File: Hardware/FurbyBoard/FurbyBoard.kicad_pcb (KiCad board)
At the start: 4 copper layers, 68.8 x 74.6 mm, 154 parts, among them J1 USB-C 16P, J11 J_EXP: header de expansión 2 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, J2 BAT+, J3 BAT-, J5 Micro I2S (SD, GND, SCK, WS, 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, J6 FPC 24P 0.5, J7 Frente: IR (emisor ×2, recept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, J8 Inclinación ×3, lengua ×2, al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, J9 Encoder ×3, leva ×2, barriga 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, Q1 SI7615ADN, Q3 AO3400A, SW1 RESET, SW2 BOOT, U1 USBLC6-2SC6, U10 TCA9535PWR, U11 SN74LVC1G17DBVR, U2 BQ24073RGTR, U3 TPS63802DLAR, U4 ESP32-S3-WROOM-1-N16R8, U5 TPS61089RNRR, U6 DRV8231ADSGR, U7 MAX98357AETE+T, U8 ME6211C28M5G-N, U9 ME6211C12M5G-N

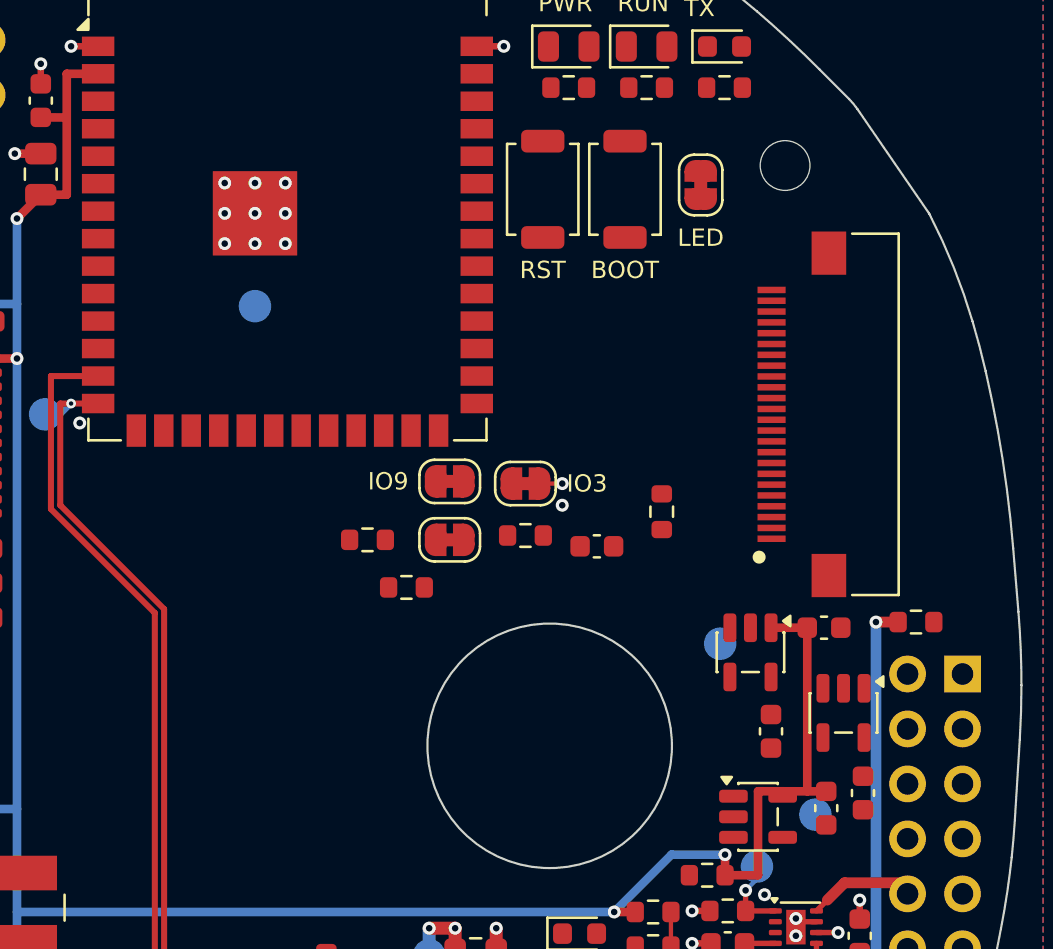
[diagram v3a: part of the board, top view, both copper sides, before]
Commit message: Feature: rutado del bus DVP de la cámara y del abanico de J6
Bus DVP J6 -> U4 en F.Cu, rutado de río sin cruces: Y2-Y5 en escalera
entre SW1 y la columna de pads a los pines 31-34; los ocho restantes
bajan a 45° a una banda de paso 0,3 (y -81,8…-83,9) y entran en los
pines 18-25 por orden. Los pines no DVP de J6 salen por el este bajo el
cuerpo a una columna de vías (GND, DVDD, PWDN, SCL, SDA, GND) o por el
oeste (2V8, RST a R35/C31); 3V3 del pin 11, de R35 y de R18 por una
fila de In2 hasta la vía de R35 y por B.Cu a U8.1. CAM_DVDD por In2
bordeando J9 hasta U9.5/C29 (TP11 en B); CAM_2V8 por In2 a U8.5/C28 y
U9.1 (TP10 en B); CAM_EN con sus vías junto a U8.3 y U9.3; BOOT de pin
27 a R18 y por In2 a SW2. Retorno de GND a <= 1 mm en cada vía CAM_*.

Colocación: JP1/JP2 en fila bajo la banda (y -85,1), JP3 a 270° al
este, R29/R30 debajo, R18 junto al pin 27, C31 junto a R35, SW1/SW2
0,4/0,2 mm al este para dejar paso a la escalera; C29 alineado con
U9.5. Puentes de soldadura: IPROPI_IO/MOT_IN*_IO desde los pines 15-17
por In2 y B.Cu (IPROPI_IO), IPROPI por In2 (x -54,7) a JP3.

DRU: cuello de 0,15 dentro del patio de J6 (pads de 0,3 a 0,5 mm de
paso, como J1), para que el 3V3 del pin 11 y el bus de 0,15 pasen.

Puerta D: DRC 0 con paridad 0 (5 avisos de vías pendientes de unir en
los bloques siguientes), revisar-rutado 0 errores, PNG revisados del
pasillo de la cámara (F, In2, B) y de la zona J6/U8/U9.

Co-Authored-By: Claude Fable 5.1 <noreply@anthropic.com>
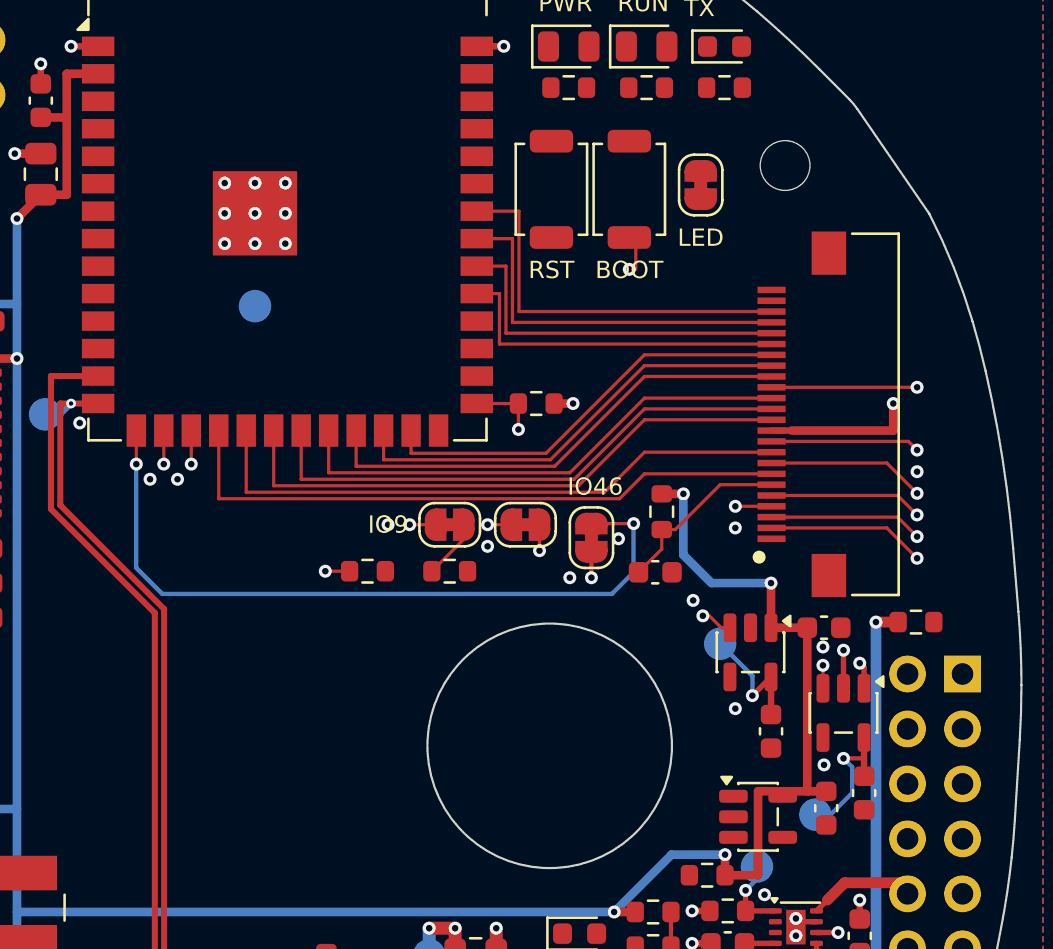
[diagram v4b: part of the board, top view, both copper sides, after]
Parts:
- moved R18 6.12 mm to (158.5, 39.5)
- moved R29 4.07 mm to (154.5, 47.2)
- moved JP3 3.94 mm to (161.1, 45.7), turned to -90 degrees
- moved JP2 3.57 mm to (158.0, 45.1)
- moved C31 2.95 mm to (164.0, 47.3)
- moved JP1 2.00 mm to (154.5, 45.1)
- moved R30 1.95 mm to (150.7, 47.2)
- moved SW1 0.40 mm to (159.2, 29.6)
- moved SW2 0.20 mm to (162.8, 29.6)
- moved C29 0.05 mm to (173.7, 57.5)
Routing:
- net 3V3: track 172.7 -> 209.9 mm, vias 10 -> 14
- net IPROPI_IO: track 0.00 -> 34.4 mm, vias 0 -> 2
- net CAM_DVDD: track 0.00 -> 29.7 mm, vias 0 -> 2
- net CAM_VSYNC: track 0.00 -> 29.2 mm
- net CAM_HREF: track 0.00 -> 27.9 mm
- net CAM_Y9: track 0.00 -> 26.8 mm
- net CAM_2V8: track 0.00 -> 26.4 mm, vias 0 -> 3
- net CAM_XCLK: track 0.00 -> 25.3 mm
- net CAM_Y8: track 0.00 -> 23.8 mm
- net CAM_Y7: track 0.00 -> 22.6 mm
- net CAM_PCLK: track 0.00 -> 21.1 mm
- net MOT_IN2_IO: track 0.00 -> 21.1 mm, vias 0 -> 2
- net CAM_Y6: track 0.00 -> 19.6 mm
- net CAM_Y4: track 0.00 -> 18.3 mm
- net CAM_Y3: track 0.00 -> 17.5 mm
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
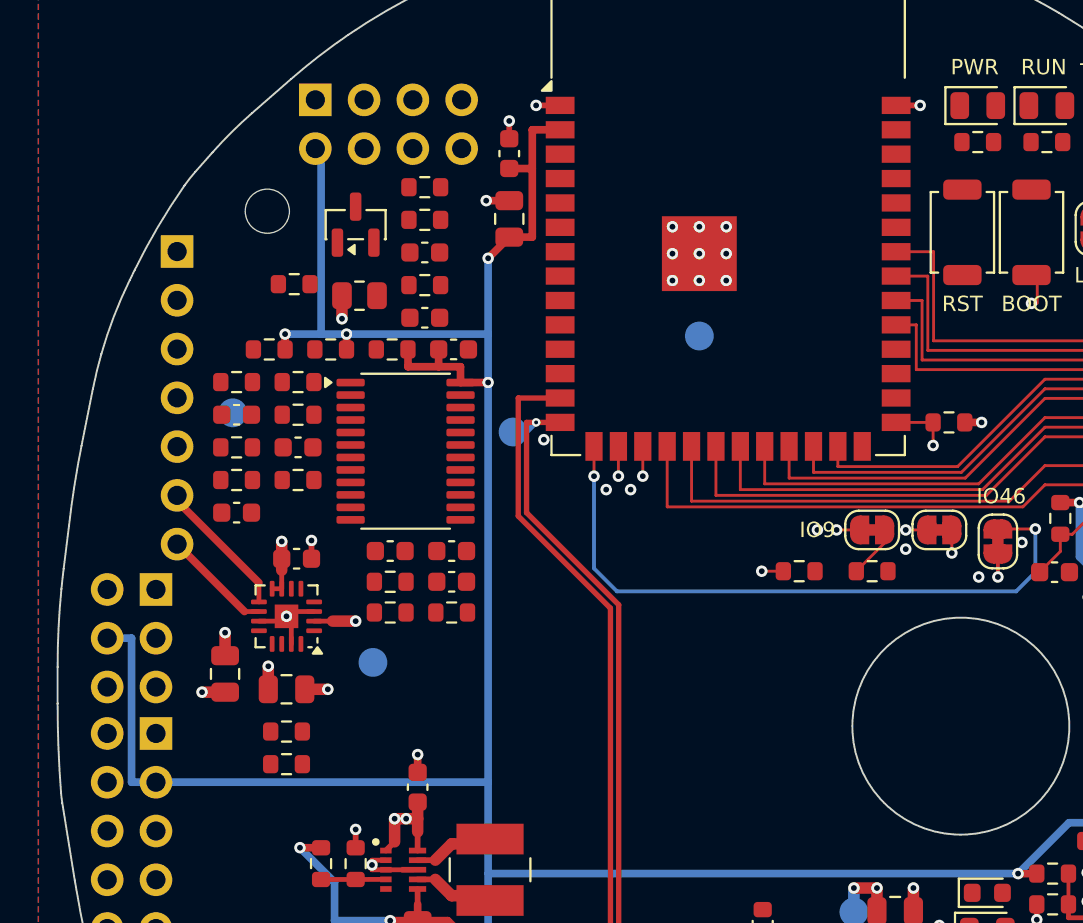
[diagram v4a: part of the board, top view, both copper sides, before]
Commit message: Feature: rutado del I2S, el I2C, EXP_INT, EN y AMP_SD de la FurbyBoard
Los pines 3-10 de la columna oeste del módulo bajan a vías bajo el
cuerpo (o al oeste del pad en WS y DIN) con retorno de GND. I2S por In2
en cuatro columnas anidadas y filas y -87,0…-88,2 hasta J5.1 (DIN),
U7.14 (WS, vía bajo C25 desde el oeste), U7.16 (BCLK, vía al este de
C25) y U7.1 (DOUT, TP9 en B); BCLK y WS siguen en F.Cu a R31/R32 (a
180°) y SCK_MIC/WS_MIC en F.Cu a J5.3/J5.4 (WS_MIC bordea J5 y J11 por
el oeste). I2C por In2 a U10.22/23 (vías al este del tronco de B.Cu)
y por B.Cu a R36/R37 (intercambiados para que las filas aniden);
EXP_INT por In2 (y -66,2, columna x -84,8) a U10.1 y R38.1; EN por In2
a R17/C11 y a SW1; AMP_SD en F.Cu. J7.5 se alimenta de 3V3 por In2
(x -93,85) para dejar libre B.Cu; TP2 bajo el par USB; C25.2 con vía al
sur (retorno de la vía de WS).

Puerta D: DRC 0 con paridad 0 (5 avisos de vías de I2C/CAM pendientes
de unir en el bloque siguiente), revisar-rutado 0 errores, PNG
revisados de la zona oeste (F, In2, B) y de U7/J5 (F, In2).

Co-Authored-By: Claude Fable 5.1 <noreply@anthropic.com>
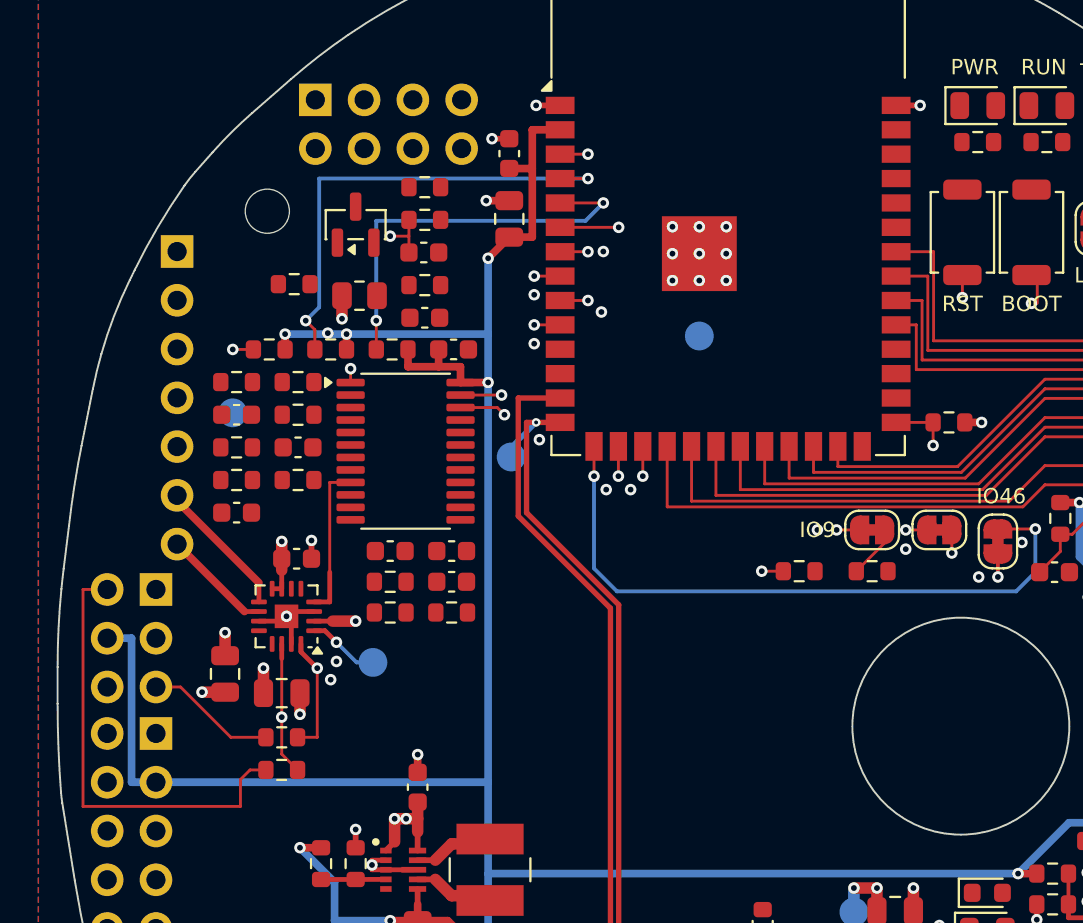
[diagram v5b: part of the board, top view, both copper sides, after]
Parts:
- moved R36 3.20 mm to (126.3, 35.7)
- moved R37 3.20 mm to (129.5, 35.7)
- moved TP2 1.30 mm to (135.7, 41.3)
- moved R31 0.39 mm to (123.8, 55.9), turned to 180 degrees
- moved R32 0.39 mm to (123.8, 57.6), turned to 180 degrees
- moved C25 0.32 mm to (123.8, 53.6)
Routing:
- net EN: track 0.00 -> 51.8 mm, vias 0 -> 3
- net I2S_WS: track 0.00 -> 50.9 mm, vias 0 -> 2
- net I2S_BCLK: track 0.00 -> 43.5 mm, vias 0 -> 2
- net I2C_SDA: track 7.10 -> 48.9 mm, vias 1 -> 4
- net I2C_SCL: track 7.10 -> 45.8 mm, vias 1 -> 4
- net EXP_INT: track 0.00 -> 38.3 mm, vias 0 -> 3
- net I2S_DOUT: track 0.00 -> 36.1 mm, vias 0 -> 2
- net I2S_DIN: track 0.00 -> 35.4 mm, vias 0 -> 1
- net I2S_WS_MIC: track 0.00 -> 23.7 mm
- net AMP_SD: track 0.00 -> 8.12 mm
- net I2S_SCK_MIC: track 0.00 -> 6.81 mm
- net 3V3: track 209.9 -> 210.8 mm, vias 14 -> 15
- net USB_DP: track 57.2 -> 58.1 mm
- net GND: track 68.6 -> 68.4 mm, vias 77 -> 83

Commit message: Feature: rutado del sensado (VBAT_SNS, LIGHT, ENC_PT), VBUS a J11 y BAT_PAD
VBAT_SNS: pin 39 -> vía bajo el módulo, In2 por y -64,26, x -78,0 y
x -80,6 (único paso libre entre las filas del I2S y las vías de los
pines 15-17) y diagonal hasta la vía junto a R13.2; divisor R13/R14/C5
encadenado en F.Cu. LIGHT: pin 38 -> vía, B.Cu por y -64,0 hasta J7.6
(THT) y por In2 a la vía junto a C40.1 (C40 a 180°). ENC_PT: U11.2 <->
R52.1 en F.Cu y vía a In2 por el hueco entre las filas de pads de J9
hasta J9.1. VBUS a J11.4 por B.Cu (diagonal larga bajo los
convertidores). BAT_PAD de J2 a Q1.5 (0,8). Zona BAT hasta y -112,3
(conexión sólida a los pines 2/3 de U2), C4 al este, vía de GND del
pin 4 de U2 a (-63,6; -113,6), retorno de BQ_TS en (-65,65; -114,45) y
BQ_TS por In2 con salida en diagonal: la zona BAT queda en un solo
polígono. Retorno de GND a <= 1 mm en cada vía de red crítica.

Puerta D: DRC 0 con paridad 0 (5 avisos de vías de I2C/CAM pendientes
de unir), revisar-rutado 0 errores, PNG revisados (NE del módulo, J7,
J9/U11, cargador y VBUS a J11).

Co-Authored-By: Claude Fable 5.1 <noreply@anthropic.com>
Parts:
- moved C4 0.85 mm to (156.1, 74.5)
- turned C40 to 180 degrees
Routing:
- net VBAT_SNS: track 0.00 -> 71.9 mm, vias 0 -> 2
- net LIGHT: track 0.00 -> 45.3 mm, vias 0 -> 2
- net VBUS: track 28.3 -> 54.8 mm
- net ENC_PT: track 0.00 -> 21.0 mm, vias 0 -> 1
- net BAT_PAD: track 0.00 -> 2.44 mm
- net BQ_TS: track 20.8 -> 19.7 mm
- net BAT: track 19.6 -> 18.6 mm
- net GND: track 68.4 -> 68.8 mm, vias 83 -> 87

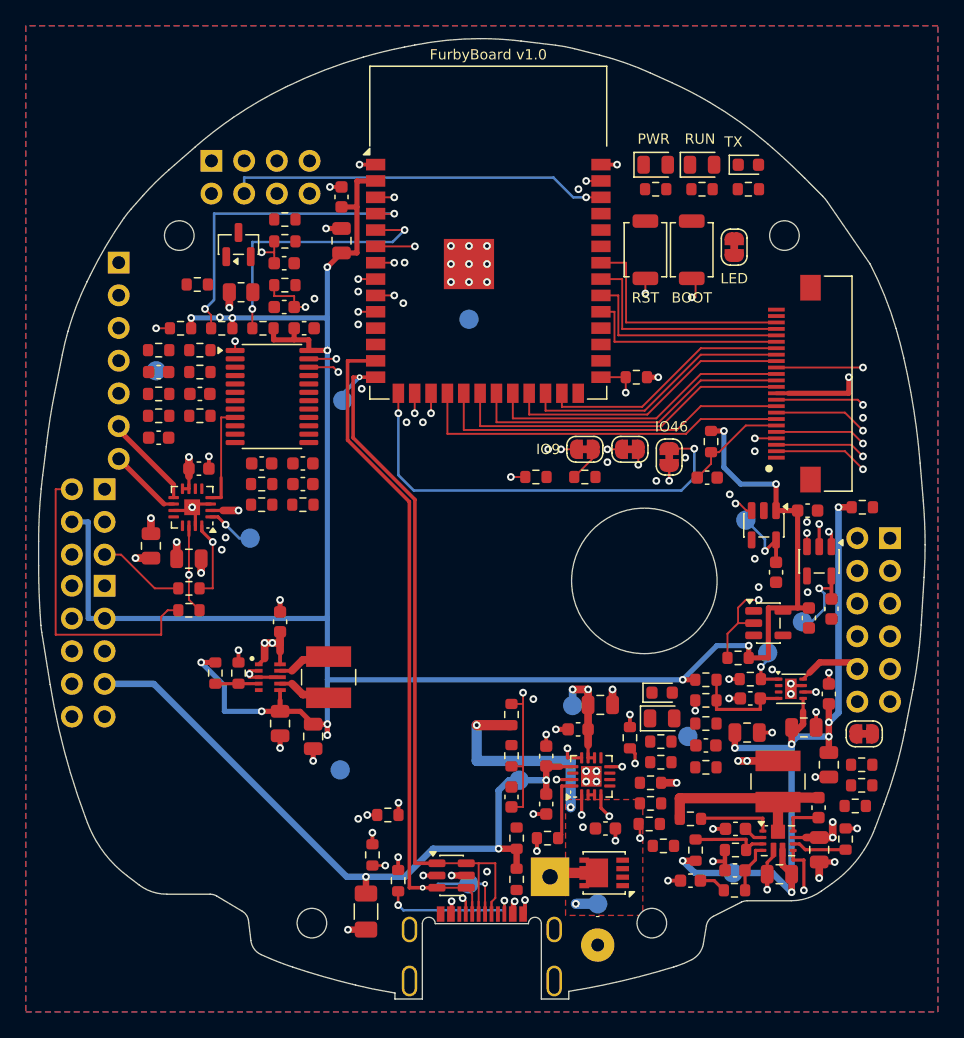
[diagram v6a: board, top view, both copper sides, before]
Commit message: Feature: rutado de las vías de GND de desacoplos y VSYS; placa regenerada solo desde los scripts
- rutas_fijas.py: vías de GND de C28, U8, C33, C11, C31, R55, C39, U11, R14, SW1, SW2, J1,
  C35, C40, JP5 y R53 (pads con hueco); los pads sin sitio quedan anotados para el relleno.
- FurbyBoard.kicad_pcb regenerado con gen_pcb.py sin --ses: se descartan las pistas que
  Freerouting había importado (decisión: el rutado restante se hace a mano).
- 3V3 a 0,4 mm también en la clase de red (params.py, .kicad_pro), como en el .kicad_dru.
- TP11 1,5 mm al oeste (R19) para liberar la leyenda de J9; J9 rotulado M2/M1 como en el esquema.
- pcb-toolkit.toml: `criticas` con las señales del bus DVP en vez de CAM_* (justificado en NOTAS.md).
- NOTAS.md (decisiones del rutado) y TEST-PLAN.md (posición real de los TP) al día.

Puerta D parcial: revisar-rutado 0 errores (77 avisos de cuello, entradas asimétricas y
rodeos heredados, a revisar en E1); DRC paridad 0, 5 vías colgantes de redes aún sin rutar
(CAM_EN, CAM_PWDN, I2C a J6); 83 sin unir pendientes del rutado a mano.

Co-Authored-By: Claude Opus 5.5 (1M context) <noreply@anthropic.com>
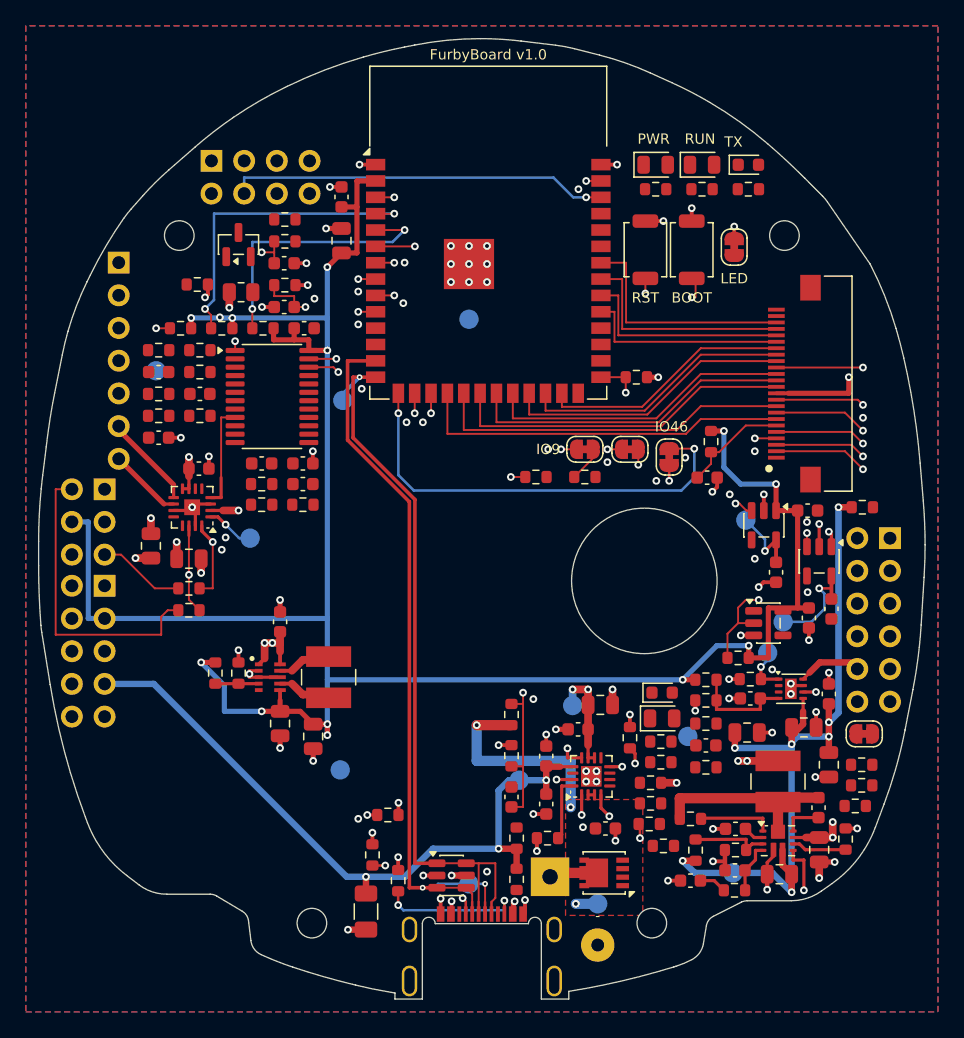
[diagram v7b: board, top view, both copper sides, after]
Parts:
- moved TP11 1.50 mm to (169.9, 58.5)
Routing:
- net GND: track 68.8 -> 86.1 mm, vias 87 -> 102
- net CAM_DVDD: track 29.7 -> 31.2 mm
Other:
- board text added: "EN+"
- board text added: "M1"
- board text removed: "M2"
